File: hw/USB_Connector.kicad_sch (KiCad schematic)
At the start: 9 parts, among them J1 USB_C_Receptacle_USB2.0_16P, U4 SRV05-4

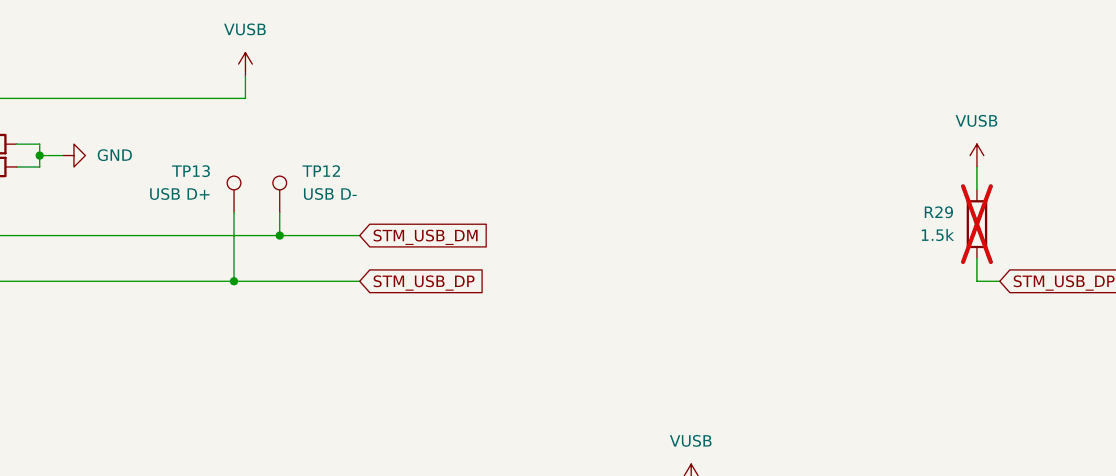
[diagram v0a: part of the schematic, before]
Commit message: added new pcb design, ERC errors not fixed yet
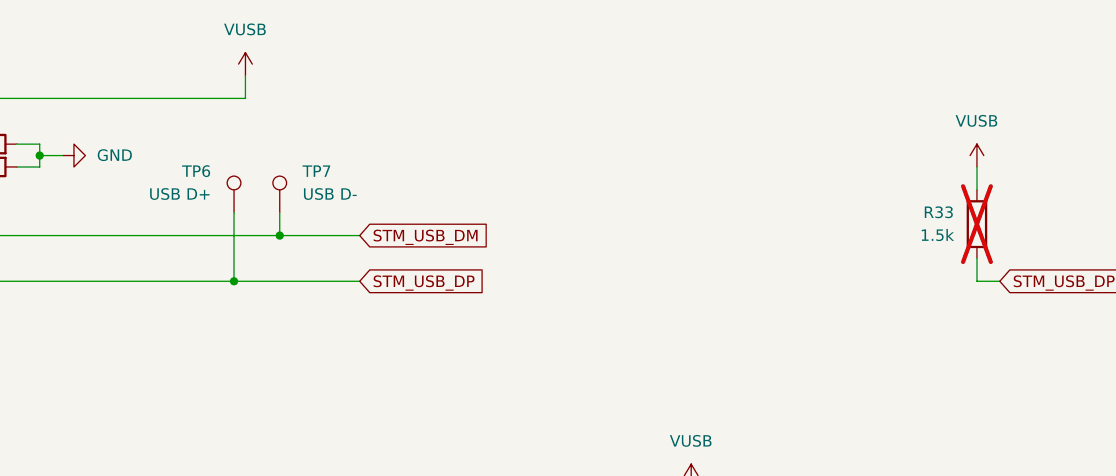
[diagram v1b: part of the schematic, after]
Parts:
- renumbered R29 to R33, TP13 to TP6, TP12 to TP7
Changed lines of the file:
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@@
 		(dnp no)
 		(fields_autoplaced yes)
-		(property "Reference" "TP12"
+		(property "Reference" "TP7"
 			(at 168.91 71.6279 0)
 			(effects
@@
 			(project "Midi Expressor"
 				(path "/1e7cbae1-0003-4e27-ba62-2dd55b10f4f2/e1936ef5-b760-4ebe-803c-fa6bc7a213ac"
-					(reference "TP12")
+					(reference "TP7")
 					(unit 1)
 				)
@@
 		(dnp yes)
 		(fields_autoplaced yes)
-		(property "Reference" "R29"
+		(property "Reference" "R33"
 			(at 241.3 76.1999 0)
 			(effects
@@
 			(project "Midi Expressor"
 				(path "/1e7cbae1-0003-4e27-ba62-2dd55b10f4f2/e1936ef5-b760-4ebe-803c-fa6bc7a213ac"
-					(reference "R29")
+					(reference "R33")
 					(unit 1)
 				)
@@
 		(on_board yes)
 		(dnp no)
-		(property "Reference" "TP13"
+		(property "Reference" "TP6"
 			(at 158.75 71.6279 0)
 			(effects
@@
 			(project "Midi Expressor"
 				(path "/1e7cbae1-0003-4e27-ba62-2dd55b10f4f2/e1936ef5-b760-4ebe-803c-fa6bc7a213ac"
-					(reference "TP13")
-					(unit 1)
-				)
+					(reference "TP6")
+					(unit 1)
+				)
